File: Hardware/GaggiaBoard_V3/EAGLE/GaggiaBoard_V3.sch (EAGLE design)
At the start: 75 parts, among them IC1 LD117AS33TR, J1 4PIN, J10 PIN262409-1, J11 PIN262409-1, J12 PIN262409-1, J13 PIN262409-1, J2 Vertical Qwiic Connector, J27 6PIN, J5 2PIN, J6 3PIN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

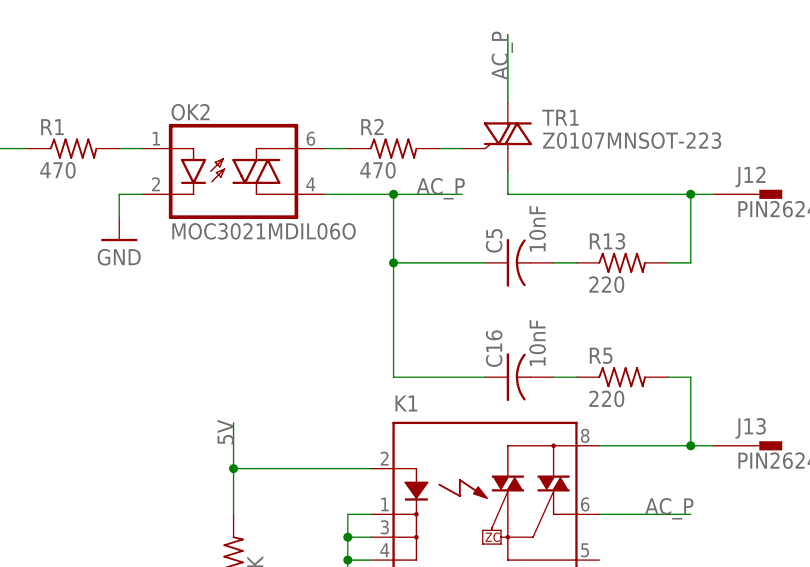
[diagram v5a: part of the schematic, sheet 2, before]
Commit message: Faston drill fix
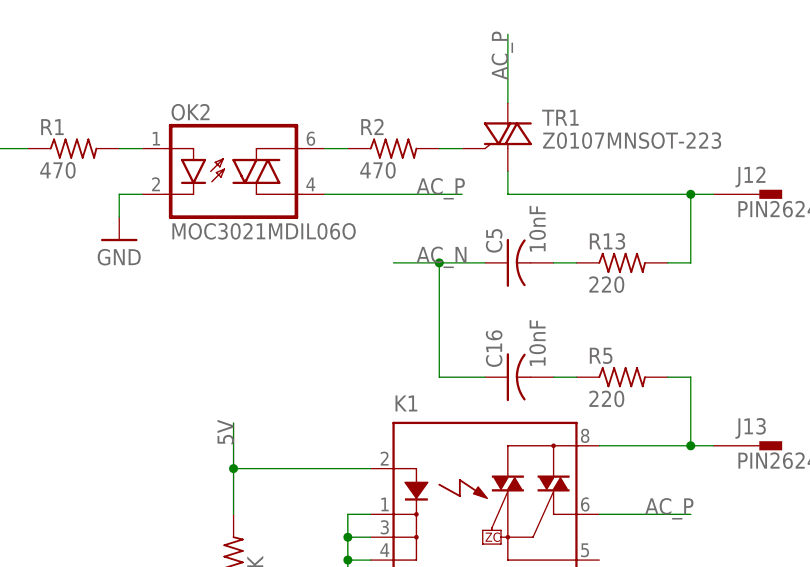
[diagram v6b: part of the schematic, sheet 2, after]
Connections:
- net AC_N: now also C16.1, C5.1
- net AC_P: no longer C16.1, C5.1
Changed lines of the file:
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@@
 <part name="MARK5" library="adafruit" library_urn="urn:adsk.eagle:library:420" deviceset="FIDUCIAL" device="" package3d_urn="urn:adsk.eagle:package:6240632/1" override_package3d_urn="urn:adsk.eagle:package:36462355/4" override_package_urn="urn:adsk.eagle:footprint:6239986/1"/>
 <part name="MARK6" library="adafruit" library_urn="urn:adsk.eagle:library:420" deviceset="FIDUCIAL" device="" package3d_urn="urn:adsk.eagle:package:6240632/1" override_package3d_urn="urn:adsk.eagle:package:36462288/4" override_package_urn="urn:adsk.eagle:footprint:6239986/1"/>
-<part name="J11" library="con-faston" library_urn="urn:adsk.eagle:library:144" deviceset="PIN2" device="62409-1" package3d_urn="urn:adsk.eagle:package:6760/1" override_package3d_urn="urn:adsk.eagle:package:36461311/2" override_package_urn="urn:adsk.eagle:footprint:6751/1">
+<part name="J11" library="con-faston" deviceset="PIN2" device="62409-1" package3d_urn="urn:adsk.eagle:package:39428999/1" override_package3d_urn="urn:adsk.eagle:package:36461311/2" override_package_urn="urn:adsk.eagle:footprint:6751/1" override_locally_modified="yes">
 <attribute name="LCSC" value="C86495"/>
 </part>
-<part name="J10" library="con-faston" library_urn="urn:adsk.eagle:library:144" deviceset="PIN2" device="62409-1" package3d_urn="urn:adsk.eagle:package:6760/1" override_package3d_urn="urn:adsk.eagle:package:36461296/2" override_package_urn="urn:adsk.eagle:footprint:6751/1">
+<part name="J10" library="con-faston" deviceset="PIN2" device="62409-1" package3d_urn="urn:adsk.eagle:package:39428999/1" override_package3d_urn="urn:adsk.eagle:package:36461296/2" override_package_urn="urn:adsk.eagle:footprint:6751/1" override_locally_modified="yes">
 <attribute name="LCSC" value="C86495"/>
 </part>
-<part name="J12" library="con-faston" library_urn="urn:adsk.eagle:library:144" deviceset="PIN2" device="62409-1" package3d_urn="urn:adsk.eagle:package:6760/1" override_package3d_urn="urn:adsk.eagle:package:36461344/2" override_package_urn="urn:adsk.eagle:footprint:6751/1">
+<part name="J12" library="con-faston" deviceset="PIN2" device="62409-1" package3d_urn="urn:adsk.eagle:package:39428999/1" override_package3d_urn="urn:adsk.eagle:package:36461344/2" override_package_urn="urn:adsk.eagle:footprint:6751/1" override_locally_modified="yes">
 <attribute name="LCSC" value="C86495"/>
 </part>
-<part name="J13" library="con-faston" library_urn="urn:adsk.eagle:library:144" deviceset="PIN2" device="62409-1" package3d_urn="urn:adsk.eagle:package:6760/1" override_package3d_urn="urn:adsk.eagle:package:36461343/2" override_package_urn="urn:adsk.eagle:footprint:6751/1">
+<part name="J13" library="con-faston" deviceset="PIN2" device="62409-1" package3d_urn="urn:adsk.eagle:package:39428999/1" override_package3d_urn="urn:adsk.eagle:package:36461343/2" override_package_urn="urn:adsk.eagle:footprint:6751/1" override_locally_modified="yes">
 <attribute name="LCSC" value="C86495"/>
 </part>
@@
 <pinref part="R21" gate="G$1" pin="1"/>
 </segment>
+<segment>
+<pinref part="C5" gate="G$1" pin="1"/>
+<wire x1="203.2" y1="109.22" x2="198.12" y2="109.22" width="0.1524" layer="91"/>
+<pinref part="C16" gate="G$1" pin="1"/>
+<wire x1="198.12" y1="109.22" x2="193.04" y2="109.22" width="0.1524" layer="91"/>
+<wire x1="203.2" y1="96.52" x2="198.12" y2="96.52" width="0.1524" layer="91"/>
+<wire x1="198.12" y1="96.52" x2="198.12" y2="109.22" width="0.1524" layer="91"/>
+<junction x="198.12" y="109.22"/>
+<label x="195.58" y="109.22" size="1.778" layer="95"/>
+</segment>
 </net>
 <net name="AC_P" class="0">
@@
 <wire x1="205.74" y1="127" x2="205.74" y2="134.62" width="0.1524" layer="91"/>
 <label x="205.74" y="129.54" size="1.778" layer="95" rot="R90"/>
-</segment>
-<segment>
-<pinref part="OK2" gate="G$1" pin="A1"/>
-<wire x1="185.42" y1="116.84" x2="193.04" y2="116.84" width="0.1524" layer="91"/>
-<label x="195.58" y="116.84" size="1.778" layer="95"/>
-<pinref part="C5" gate="G$1" pin="1"/>
-<wire x1="193.04" y1="116.84" x2="200.66" y2="116.84" width="0.1524" layer="91"/>
-<wire x1="203.2" y1="109.22" x2="193.04" y2="109.22" width="0.1524" layer="91"/>
-<wire x1="193.04" y1="109.22" x2="193.04" y2="116.84" width="0.1524" layer="91"/>
-<junction x="193.04" y="116.84"/>
-<pinref part="C16" gate="G$1" pin="1"/>
-<wire x1="203.2" y1="96.52" x2="193.04" y2="96.52" width="0.1524" layer="91"/>
-<wire x1="193.04" y1="96.52" x2="193.04" y2="109.22" width="0.1524" layer="91"/>
-<junction x="193.04" y="109.22"/>
 </segment>
 <segment>
@@
 <pinref part="J11" gate="-1" pin="1"/>
 </segment>
-</net>
+<segment>
+<pinref part="OK2" gate="G$1" pin="A1"/>
+<wire x1="185.42" y1="116.84" x2="200.66" y2="116.84" width="0.1524" layer="91"/>
+<label x="195.58" y="116.84" size="1.778" layer="95"/>
+</segment>
+</net>

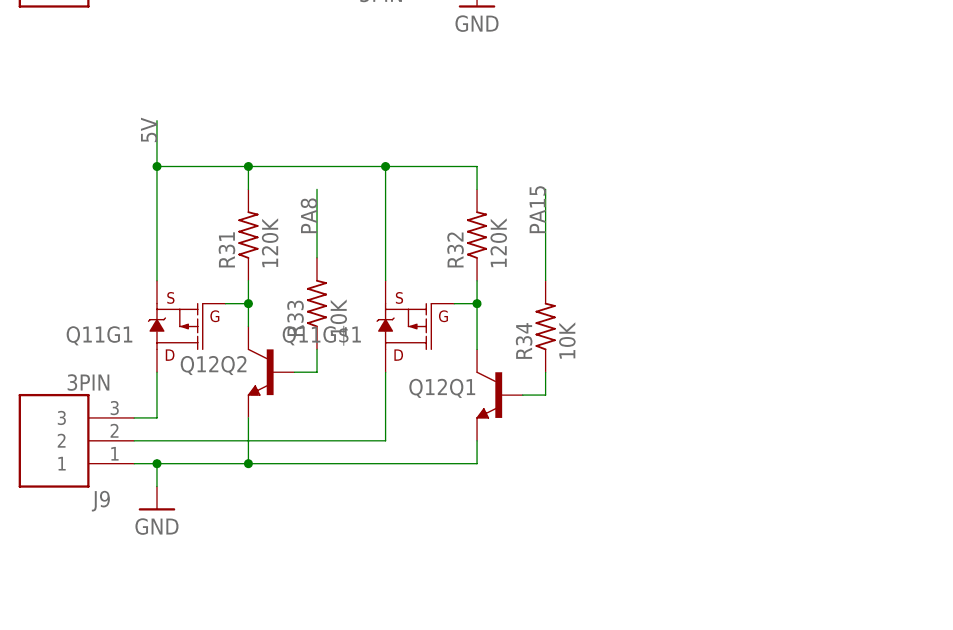
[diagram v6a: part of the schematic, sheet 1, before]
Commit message: pull downs on GPIO outputs
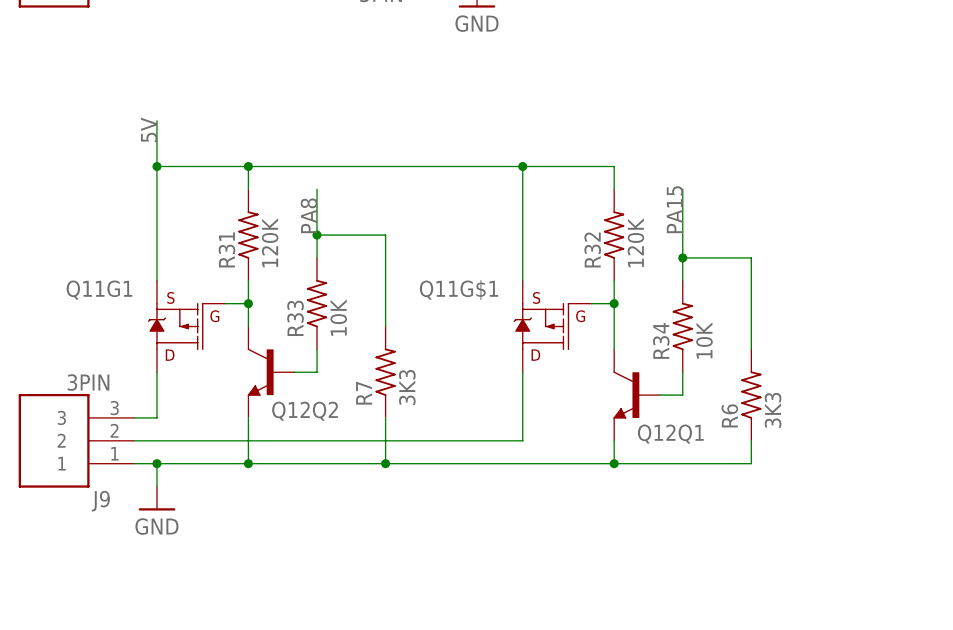
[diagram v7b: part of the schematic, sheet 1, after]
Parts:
- added R6, R7, R9: 3K3, rcl:R-US_R0603
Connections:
- net GND: now also R6.1, R7.1, R9.1
- net PA15: now also R6.2
- net PA8: now also R7.2
- net PC13: now also R9.2
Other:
- moved on the sheet: Q11G$1, Q12Q1, R32, R34

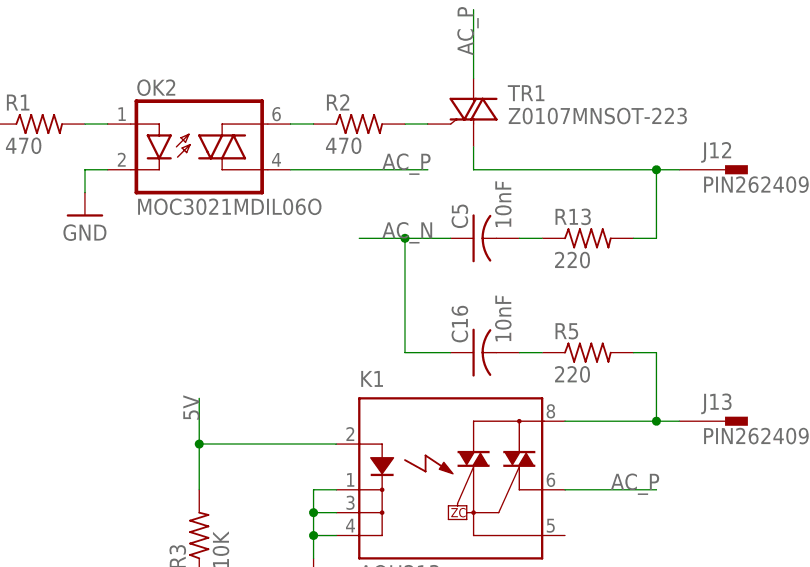
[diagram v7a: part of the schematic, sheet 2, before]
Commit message: Snubber change
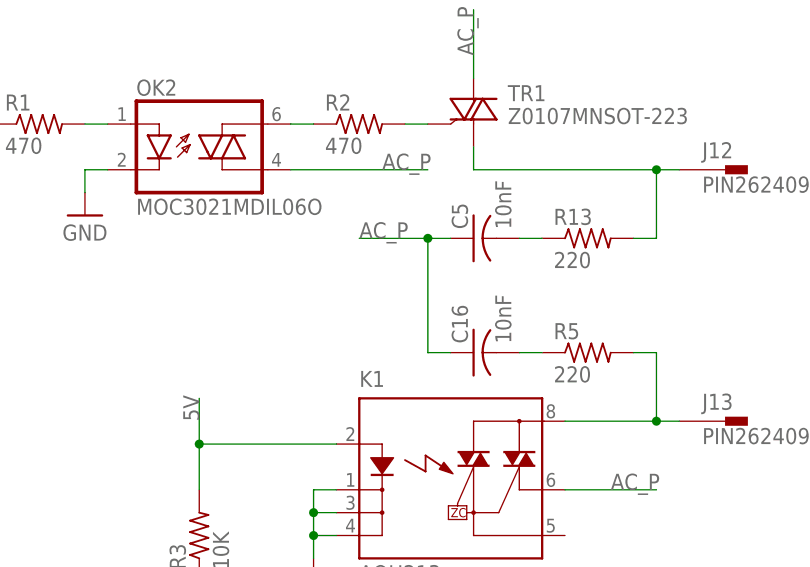
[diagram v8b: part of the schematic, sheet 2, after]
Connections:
- net AC_N: no longer C16.1, C5.1
- net AC_P: now also C16.1, C5.1
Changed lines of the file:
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@@
 <class number="0" name="default" width="0" drill="0">
+</class>
+<class number="1" name="TC" width="0" drill="0">
+<clearance class="1" value="0.508"/>
+</class>
+<class number="2" name="Analog" width="0" drill="0">
+<clearance class="2" value="0.254"/>
 </class>
 </classes>
@@
 </segment>
 </net>
-<net name="N$5" class="0">
+<net name="N$5" class="1">
 <segment>
 <pinref part="FB2" gate="G$1" pin="2"/>
@@
 </segment>
 </net>
-<net name="N$26" class="0">
+<net name="N$26" class="1">
 <segment>
 <pinref part="FB1" gate="G$1" pin="2"/>
@@
 </segment>
 </net>
-<net name="PRESSURE" class="0">
+<net name="PRESSURE" class="2">
 <segment>
 <pinref part="J6" gate="G$1" pin="3"/>
@@
 </segment>
 </net>
-<net name="N$3" class="0">
+<net name="N$3" class="1">
 <segment>
 <pinref part="FB2" gate="G$1" pin="1"/>
@@
 </segment>
 </net>
-<net name="N$4" class="0">
+<net name="N$4" class="1">
 <segment>
 <pinref part="FB1" gate="G$1" pin="1"/>
@@
 <pinref part="R21" gate="G$1" pin="1"/>
 </segment>
-<segment>
-<pinref part="C5" gate="G$1" pin="1"/>
-<wire x1="203.2" y1="109.22" x2="198.12" y2="109.22" width="0.1524" layer="91"/>
-<pinref part="C16" gate="G$1" pin="1"/>
-<wire x1="198.12" y1="109.22" x2="193.04" y2="109.22" width="0.1524" layer="91"/>
-<wire x1="203.2" y1="96.52" x2="198.12" y2="96.52" width="0.1524" layer="91"/>
-<wire x1="198.12" y1="96.52" x2="198.12" y2="109.22" width="0.1524" layer="91"/>
-<junction x="198.12" y="109.22"/>
-<label x="195.58" y="109.22" size="1.778" layer="95"/>
-</segment>
 </net>
 <net name="AC_P" class="0">
@@
 <label x="195.58" y="116.84" size="1.778" layer="95"/>
 </segment>
-</net>
+<segment>
+<pinref part="C5" gate="G$1" pin="1"/>
+<wire x1="203.2" y1="109.22" x2="200.66" y2="109.22" width="0.1524" layer="91"/>
+<pinref part="C16" gate="G$1" pin="1"/>
+<wire x1="200.66" y1="109.22" x2="193.04" y2="109.22" width="0.1524" layer="91"/>
+<wire x1="203.2" y1="96.52" x2="200.66" y2="96.52" width="0.1524" layer="91"/>
+<wire x1="200.66" y1="96.52" x2="200.66" y2="109.22" width="0.1524" layer="91"/>
+<junction x="200.66" y="109.22"/>
+<label x="193.04" y="109.22" size="1.778" layer="95"/>
+</segment>
+</net>
